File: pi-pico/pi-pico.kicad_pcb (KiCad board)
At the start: 2 copper layers, 124 x 44 mm, 29 parts, among them J1 BT A, J10 ENC L, J11 ENC R, J2 BT B, J3 BT C, J4 BT D, J5 FX L, J6 FX R, J7 Start, J8 POT L, J9 POT R, Q1 BSS138, Q2 BSS138, Q3 BSS138, Q4 BSS138, Q5 BSS138, Q6 BSS138, Q7 BSS138, SW1 SW_DIP_x01

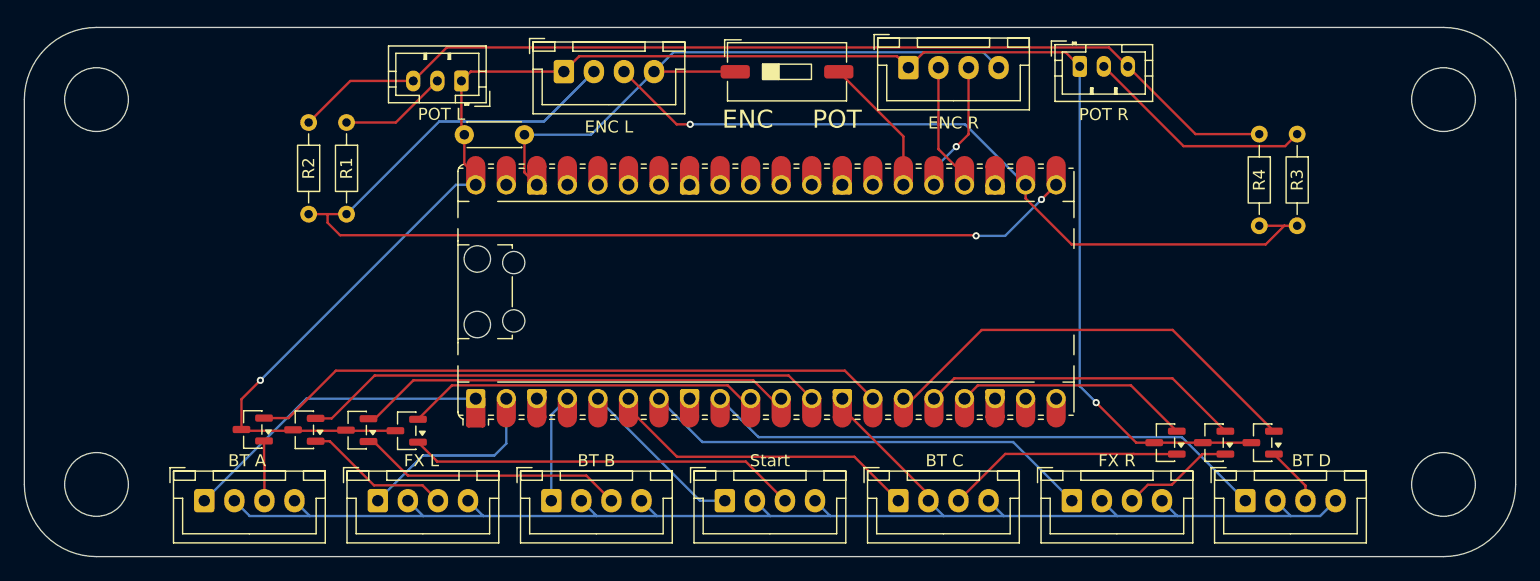
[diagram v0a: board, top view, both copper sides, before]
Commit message: Refactor readme
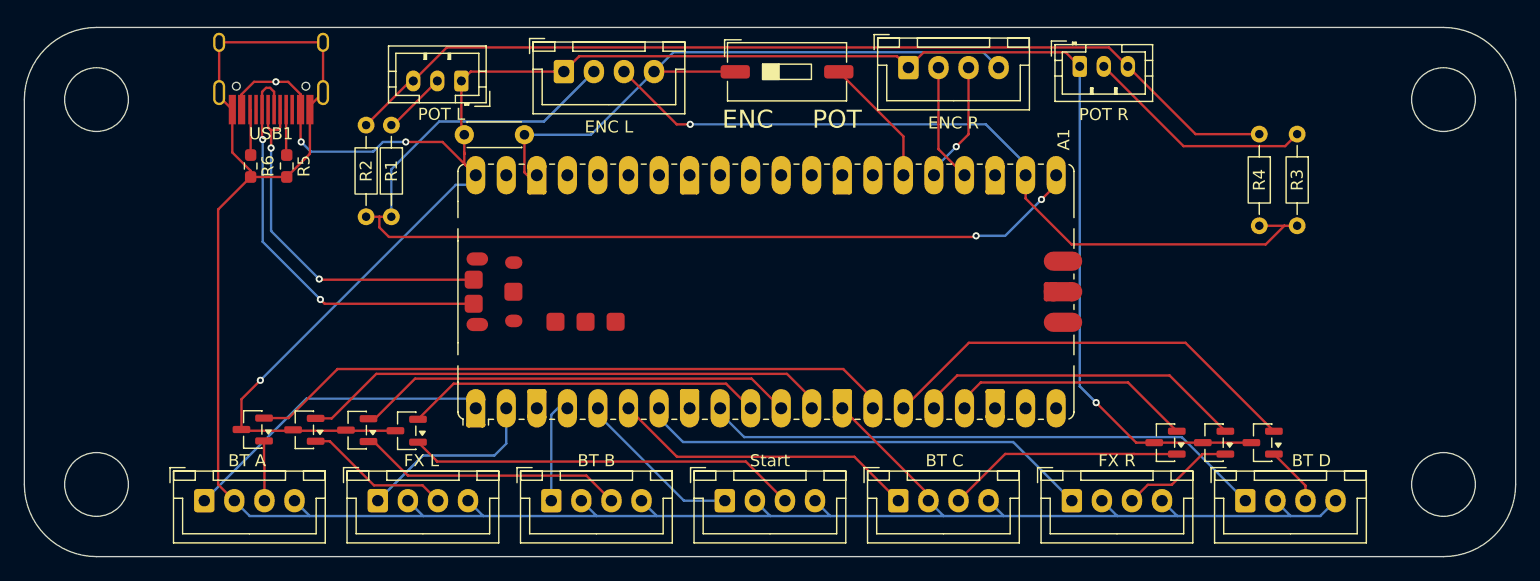
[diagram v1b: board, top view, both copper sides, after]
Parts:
- added R5: 5K1, Resistor_SMD:R_0603_1608Metric_Pad0.98x0.95mm_HandSolder, F.Cu at (112.3, 83.5)
- added R6: 5K1, Resistor_SMD:R_0603_1608Metric_Pad0.98x0.95mm_HandSolder, F.Cu at (109.3, 83.5)
- added USB1: HRO-TYPE-C-31-M-12, Type-C:HRO-TYPE-C-31-M-12-HandSoldering, F.Cu at (111.0, 70.6)
- A1: footprint Module:RaspberryPi_Pico_Common_Unspecified -> Module:RaspberryPi_Pico_SMD
- moved R2 4.78 mm to (118.9, 80.1)
- moved R1 3.73 mm to (121.0, 80.1)
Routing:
- net GND: track 179.1 -> 244.0 mm
- net Net-(A1-USB_DP): track 0.00 -> 34.9 mm, vias 0 -> 2
- net Net-(A1-USB_DM): track 0.00 -> 31.4 mm, vias 0 -> 2
- net +5V: track 147.0 -> 174.5 mm, vias 2 -> 5
- net Net-(A1-GPIO16): track 92.1 -> 85.5 mm
- net AGND: track 84.6 -> 79.9 mm
- net Net-(USB1-CC2): track 0.00 -> 3.80 mm
- net Net-(USB1-CC1): track 0.00 -> 3.80 mm
- net Net-(J8-Pin_2): track 8.98 -> 5.34 mm
- net Net-(A1-GPIO17): track 65.3 -> 66.3 mm
- net Net-(A1-GPIO5): track 37.8 -> 38.8 mm
- net Net-(A1-GPIO11): track 37.0 -> 36.1 mm
- net Net-(A1-GPIO3): track 14.1 -> 14.8 mm
- net Net-(A1-GPIO6): track 47.2 -> 47.9 mm

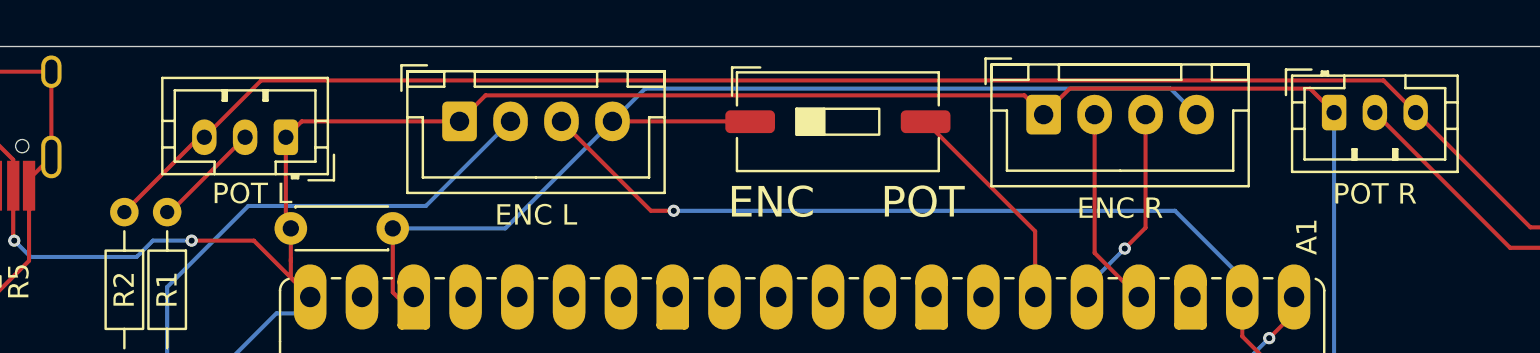
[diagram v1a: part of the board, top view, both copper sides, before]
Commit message: Rotate knob hole
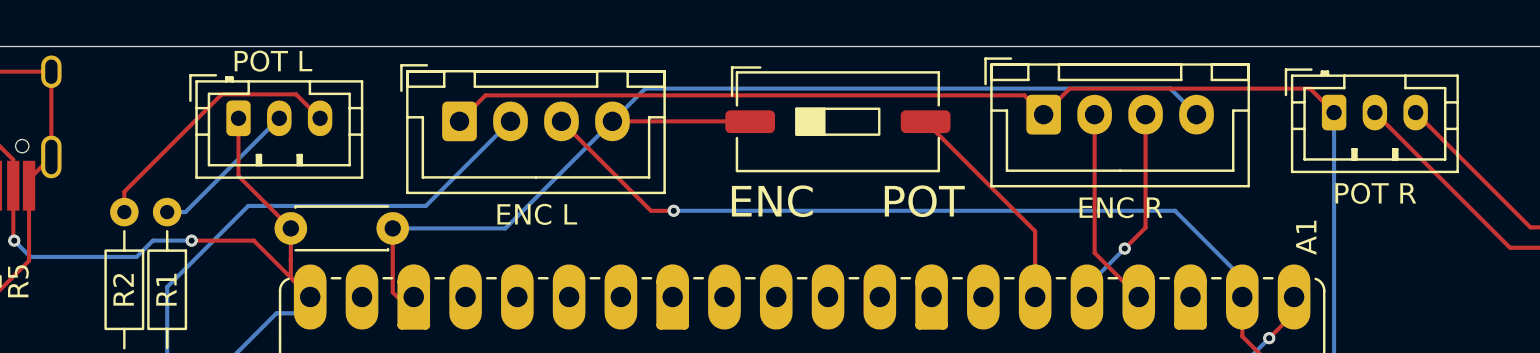
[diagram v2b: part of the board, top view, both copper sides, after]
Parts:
- moved J8 2.50 mm to (124.5, 75.5), turned to 0 degrees
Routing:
- net AGND: track 79.9 -> 26.3 mm
- net +5V: track 174.5 -> 167.5 mm
- net Net-(J8-Pin_2): track 5.34 -> 7.41 mm
